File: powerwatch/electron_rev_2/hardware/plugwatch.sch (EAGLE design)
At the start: 73 parts, among them J1 TC2030-JLINK-NL, Q1 MPSA42, T1 DMG3415, U1 MAX-M8, U2 microSD, U3 ISL29035, U37 MPU-9250, U4 NRF51822QF, U5 SAFFB1G56KB0F0A, U6 BGA725L6-ALT, U7 OPA322AIDBVT, X3 16MHz, X4 ABS05-32.768KHZ-9-T

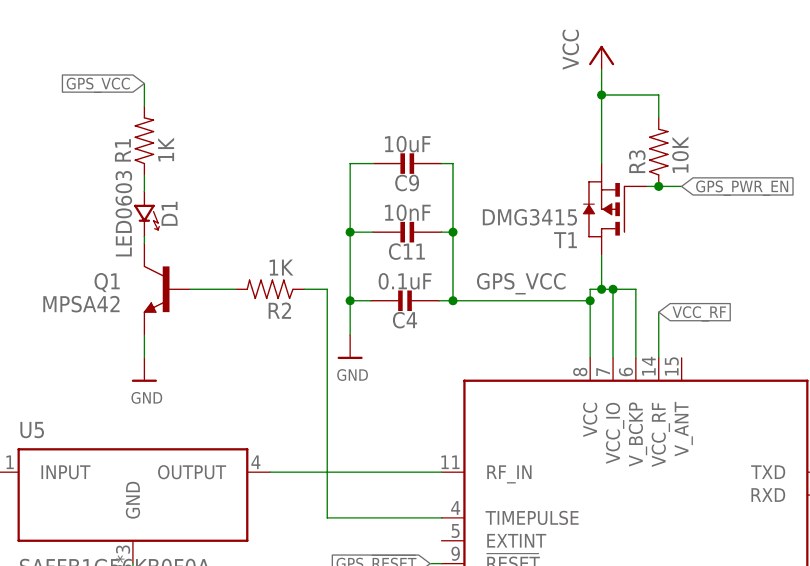
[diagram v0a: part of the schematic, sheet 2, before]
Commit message: Added part numbers and notes
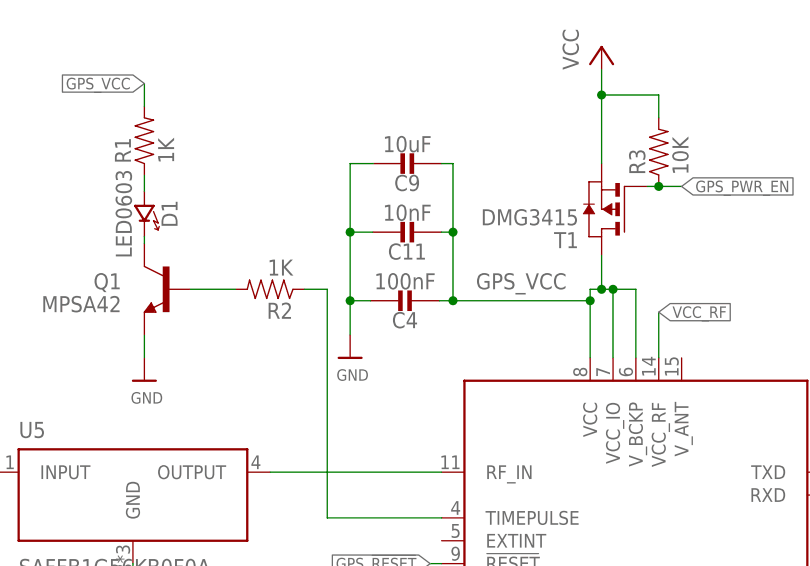
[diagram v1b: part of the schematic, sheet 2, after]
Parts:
- C1, C732: DIGIKEY (none) -> 490-10777-1-ND
- C11, C3, C5: DIGIKEY (none) -> 490-7763-1-ND
- C18: value 0.1uF -> 100nF; DIGIKEY 445-4952-1-ND -> 490-10777-1-ND
- C19, C24: DIGIKEY 490-1303-1-ND -> 490-6366-1-ND
- C2: DIGIKEY (none) -> 445-5947-1-ND
- C21: DIGIKEY 1276-1513-1-ND -> 490-14457-1-ND
- C25: DIGIKEY 445-1264-1-ND -> 490-11420-1-ND
- C4: value 0.1uF -> 100nF; DIGIKEY (none) -> 490-10777-1-ND
- C9: DIGIKEY (none) -> 490-8316-1-ND
- R1, R2: DIGIKEY (none) -> RMCF0402FT1K00CT-ND
- R10, R11, R3, R5, R6, R7, R8: DIGIKEY (none) -> RMCF0402FT10K0CT-ND
- R12: DIGIKEY RHM12.0KCDCT-ND -> RMCF0402FT12K0CT-ND
- R13: DIGIKEY RHM1.0KCECT-ND -> RMCF0402FT1K00CT-ND
- R14: DIGIKEY RHM150CDCT-ND -> RMCF0402FT150RCT-ND
- R15, R9: DIGIKEY 1276-3431-1-ND -> RMCF0402FT10K0CT-ND; MPN MF-RES-0402-10K -> (none); MPN1 RC1005F103CS -> (none)
- R4: DIGIKEY (none) -> RMCF0402FT1M00CT-ND
- T1: DIGIKEY (none) -> DMG3415UDICT-ND
- U37: DIGIKEY (none) -> 1428-1019-1-ND
- U6: DIGIKEY (none) -> BGA725L6E6327FTSA1CT-ND
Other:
- note added: "XXX: Add headers to this part number"
- note added: "XXX: Determine SD part number"
- note added: "XXX: Figure out which FB & GPS to buy"
- note added: "XXX: Find part number for GPS antenna & Inductor"
- note added: "XXX: Need to pick a purchaseable SAW"
- note added: "XXX: Need to pick a purchaseable transistor"
- note added: "XXX: Pick all of these parts"

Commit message: Schematic almost ready
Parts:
- removed Q1: MPSA42, SparkFun-DiscreteSemi:TRANSISTOR_NPNMPSA42
- removed U$3: SIP32510, chips:SIP32510
- removed U$5: CMB-6544PF, microphone:CMB-6544PF
- removed U2: microSD, SparkFun:USD-SOCKETSMD
- added A4: WRL-13678, chips:WRL-13678
- added C12, C13: 100nF, passives:CAPACITOR0402_CAP
- added C15: 330pF, passives:CAPACITOR0402_CAP
- added J2: DM3AT-SF-PEJM5, connector:DM3AT-SF-PEJM5
- added MK1: AOM-4546P-R, microphones:AOM-4546P-R
- added S1: PTS645SM43SMTR92, switches:PTS645SM43SMTR92
- added SW7: SIP3240X, signpost:SIP3240X
- added U8: MAX740XESA, chips:MAX740XESA
- A1: DIGIKEY (none) -> S7051-ND,S7051-ND
- A2: DIGIKEY (none) -> 311-1531-ND
- C10: value 1uf -> 2.2uF; device passives:CAPACITOR0402_CAP -> passives:CAP_POL1206; DIGIKEY (none) -> 718-1131-1-ND
- C6: device passives:CAPACITOR0402_CAP -> passives:CAP_POL1206; DIGIKEY (none) -> 718-1131-1-ND
- C7: value 16pF -> 4.4pF; device passives:CAPACITOR0402_CAP -> passives:CAPACITOR0603_CAP; DIGIKEY (none) -> 399-16187-1-ND
- C8: value 25uF -> 10uF; device passives:CAPACITOR0402_CAP -> passives:CAP_POL1206; DIGIKEY (none) -> 478-8481-1-ND
- L1: DIGIKEY (none) -> 490-11766-1-ND
- L2, L3: value (none) -> 1k; DIGIKEY (none) -> 490-4003-1-ND
- R1: value 1K -> 1k
- R10, R11, R3, R5: value 10K -> 10k
- R16: value 13.7K -> 3.48k; device passives:RESISTOR0402_RES -> passives:RESISTOR0603_RES; DIGIKEY (none) -> 541-3.48KHCT-ND
- R17, R18, R19: value 100K -> 100k; device passives:RESISTOR0402_RES -> passives:RESISTOR0603_RES; DIGIKEY (none) -> 541-2972-1-ND
- R2: value 1K -> 10k; DIGIKEY RMCF0402FT1K00CT-ND -> RMCF0402FT10K0CT-ND
- R20: device passives:RESISTOR0402_RES -> passives:RESISTOR0603_RES; DIGIKEY (none) -> 541-3003-1-ND
- R21: value 75K -> 270k; device passives:RESISTOR0402_RES -> passives:RESISTOR0603_RES; DIGIKEY (none) -> 541-270KHCT-ND
- R4: value 1M -> 10k; DIGIKEY RMCF0402FT1M00CT-ND -> RMCF0402FT10K0CT-ND
- R6, R7: value 10K -> 100k; DIGIKEY RMCF0402FT10K0CT-ND -> 1276-3432-1-ND
- R8: value 10K -> 150; DIGIKEY RMCF0402FT10K0CT-ND -> RMCF0402FT150RCT-ND
- U1: DIGIKEY (none) -> 672-1003-1-ND
- U5: ABACUS_TECHNOLOGIES (none) -> SAFFB1G56KB0F0A
- U7: device OPA322AIDBVT:OPA322AIDBVT -> opamps:OPA322AIDBVT
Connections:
- net GPS_!RESET renamed !GPS_RESET
- net IMU_SCL renamed SENSORS_SCL
- net IMU_SDA renamed SENSORS_SDA
- removed net N$3: C2.1, R5.2, R6.2, R7.2, R8.2, U$3.VLOAD, U2.VCC
- removed net N$37: Q1.B, R2.2
- removed net NRF_VCC: C18.1, C20.1, J1.VCC, R13.1, U4.VDD
- removed net SD_DET: R8.1, U2.CD1
- removed net SD_EN: R4.1, U$3.EN
- removed net SD_SCK: U2.SCK
- removed net SD_SS: R5.1, U2.CS
- removed net TIMEPULSE: R2.1, U1.TIMEPULSE
- new net !SAFEMODE: R8.2, S1.P$2
- new net !SD_CS: J2.DATA3-CD/CS_N, R4.1
- new net !SD_DETECT: J2.A, R6.1
- new net !WIFI_RESET: A4.!RST
- new net AUDIO_OUT: U8.OUT
- new net N$11: C13.1, U8.COM, U8.OS
- new net N$18: C2.1, J2.VCC, R2.2, R4.2, R5.2, R6.2, SW7.VLOAD
- new net N$6: C15.2, U8.CLK
- new net SD_ENABLE_POWER: R7.1, SW7.EN
- new net SD_SCLK: J2.CLK
- new net WIFI_RXD: A4.RXI
- new net WIFI_TXD: A4.TXO
- net -AMP: now also C8.CATHODE; no longer C8.2
- net A_MIC_OUT: now also C10.ANODE, U8.IN; no longer C10.2
- net GND: now also A4.GND, C12.2, C13.2, C15.1, C6.ANODE, J2.B, J2.GND, MK1.2, S1.P$1, SW7.GND, U8.GND; no longer C6.2, Q1.E, U$3.GND, U$5.V-, U2.CD2, U2.GND, U2.SHIELD1, U2.SHIELD2
- net N$2: now also U1.TIMEPULSE; no longer Q1.C
- net N$4: now also C8.ANODE, MK1.1; no longer C8.1, U$5.V+
- net N$7: now also C10.CATHODE; no longer C10.1
- net N$9: now also C6.CATHODE; no longer C6.1
- net SD_MISO: now also J2.DATA0/MISO, R5.1; no longer R7.1, U2.DO
- net SD_MOSI: now also J2.CMD/MOSI, R2.1; no longer R6.1, U2.DI
- net VCC: now also A4.3V3, A4.EN, C18.1, C20.1, J1.VCC, R13.1, R7.2, R8.1, SW7.VSUPP, U4.VDD; no longer R4.2, U$3.VSUPP
- net VCC_A_MIC: now also C12.1, U8.!SHDN, U8.VDD
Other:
- note added: "I2C Address: 0x68"
- note added: "SD Card Adapter"
- note added: "XXX: Check PCB layout section of TI doc"
- note added: "XXX: Pick an actual LED part and apply to other LEDs too"
- note added: "http://www.ti.com/lit/ug/tidu765/tidu765.pdf"
- note added: "https://cdn.sparkfun.com/datasheets/Wireless/WiFi/ESP8266ModuleV1.pdf"
- note added: "https://www.u-blox.com/sites/default/files/MAX-8-M8-FW3_HardwareIntegrationManual_%28UBX-15030059%29.pdf"
- note removed: "SD Card"
- note removed: "XXX: ADD LOW PASS FILTER"
- note removed: "XXX: Add headers to this part number"
- note removed: "XXX: Determine SD part number"
- note removed: "XXX: Figure out which FB & GPS to buy"
- note removed: "XXX: Find part number for GPS antenna & Inductor"
- note removed: "XXX: Need to pick a purchaseable SAW"
- note removed: "XXX: Need to pick a purchaseable transistor"
- note removed: "XXX: Pick all of these parts"
- moved on the sheet: C2, C7, D1, R1, R16, R17, R18, R19, R20, R21, R4, R5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

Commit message: Schematic done?
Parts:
- removed D3: BLUE, SparkFun-LED:LED0603
- added D2: LED0603, leds:LED0603
- added R22: 10k, passives:RESISTOR0402_RES
- added T2: DMG3415, zetex:PMOSSOT23
- D1: DIGIKEY (none) -> 160-1837-6-ND
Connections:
- removed net IMU_INT: R15.1, U37.INT
- new net !IMU_INT: A1.D0, R15.1, U37.INT
- new net AUDIO_PWR_EN: A1.B0, R22.1, T2.G
- net !GPS_RESET: now also A1.D4
- net !LIGHT_INT: now also A1.D1
- net !SAFEMODE: now also A1.D7
- net !SD_CS: now also A1.A2
- net !SD_DETECT: now also A1.D6
- net !WIFI_RESET: now also A1.D5
- net AUDIO_OUT: now also A1.B2
- net BLE_RXD: now also A1.C1
- net BLE_TXD: now also A1.C0
- net GND: now also A1.GND, A1.GND@2
- net GPS_PWR_EN: now also A1.D3
- net GPS_RXD: now also A1.TX
- net GPS_TXD: now also A1.RX
- net N$25: now also D2.ANODE; no longer D3.A
- net NRF_P29: now also D2.CATHODE; no longer D3.C
- net NRF_SWDIO/!RESET: now also A1.D2
- net SD_MISO: now also A1.A4
- net SD_MOSI: now also A1.A5
- net SD_SCLK: now also A1.A3
- net SENSORS_SCL: now also A1.C5
- net SENSORS_SDA: now also A1.C4
- net VCC: now also A1.3V3, R22.2, T2.S
- net VCC_A_MIC: now also T2.D
- net WIFI_RXD: now also A1.C3
- net WIFI_TXD: now also A1.C2
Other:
- note added: "Note: GPIO choices are arbitrary"
- note added: "Note: Pin choices are arbitrary"
- note removed: "XXX: Pick an actual LED part and apply to other LEDs too"
- note removed: "XXX: Pick real pins for me"
- moved on the sheet: C10, C12, C13, C15, C6, C7, C8, MK1, R16, R17, R18, R19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

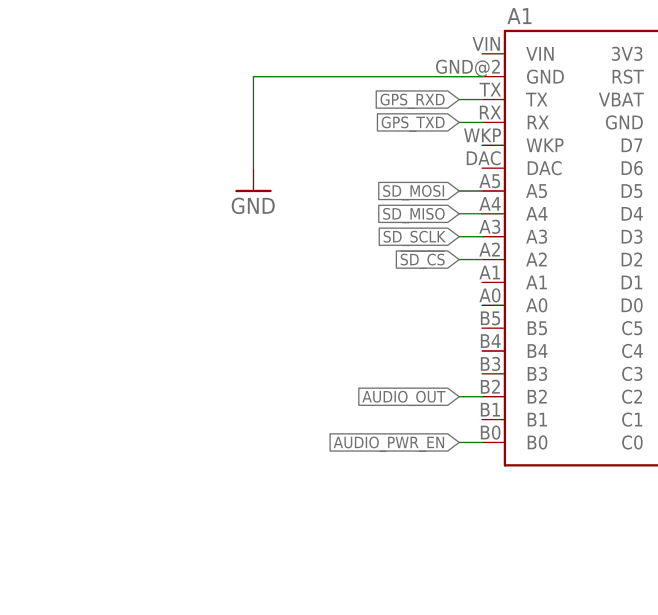
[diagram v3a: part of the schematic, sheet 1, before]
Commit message: locked key parts on board, added LED
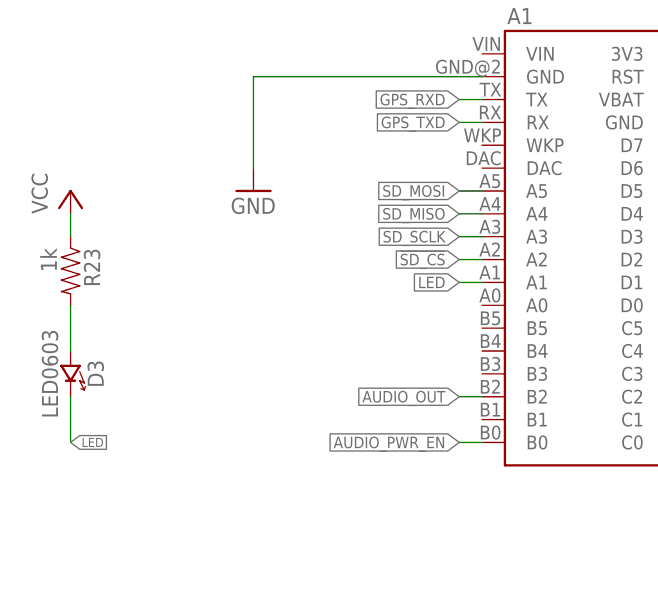
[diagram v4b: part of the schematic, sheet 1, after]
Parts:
- added D3: LED0603, leds:LED0603
- added R23: 1k, passives:RESISTOR0402_RES
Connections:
- new net LED: A1.A1, D3.CATHODE
- new net N$3: D3.ANODE, R23.2
- net VCC: now also R23.1
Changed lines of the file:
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@@
 <part name="P+13" library="supply1" library_urn="urn:adsk.eagle:library:371" deviceset="VCC" device=""/>
 <part name="D2" library="leds" deviceset="LED" device="0603"/>
+<part name="R23" library="passives" deviceset="RESISTOR" device="0402_RES" value="1k">
+<attribute name="DIGIKEY" value="RMCF0402FT1K00CT-ND"/>
+</part>
+<part name="P+14" library="supply1" library_urn="urn:adsk.eagle:library:371" deviceset="VCC" device=""/>
+<part name="D3" library="leds" deviceset="LED" device="0603"/>
 </parts>
 <sheets>
@@
 <instance part="GND32" gate="1" x="121.92" y="127"/>
 <instance part="GND33" gate="1" x="38.1" y="132.08"/>
+<instance part="R23" gate="G$1" x="17.78" y="121.92" rot="R270">
+<attribute name="DIGIKEY" x="17.78" y="121.92" size="1.27" layer="96" rot="R270" display="off"/>
+</instance>
+<instance part="P+14" gate="VCC" x="17.78" y="132.08"/>
+<instance part="D3" gate="G$1" x="17.78" y="111.76" rot="R270"/>
 </instances>
 <busses>
@@
 <wire x1="93.98" y1="147.32" x2="93.98" y2="149.86" width="0.1524" layer="91"/>
 </segment>
+<segment>
+<pinref part="R23" gate="G$1" pin="1"/>
+<pinref part="P+14" gate="VCC" pin="VCC"/>
+<wire x1="17.78" y1="127" x2="17.78" y2="129.54" width="0.1524" layer="91"/>
+</segment>
 </net>
 <net name="!SAFEMODE" class="0">
@@
 </segment>
 </net>
+<net name="N$3" class="0">
+<segment>
+<pinref part="R23" gate="G$1" pin="2"/>
+<pinref part="D3" gate="G$1" pin="ANODE"/>
+<wire x1="17.78" y1="114.3" x2="17.78" y2="119.38" width="0.1524" layer="91"/>
+</segment>
+</net>
+<net name="LED" class="0">
+<segment>
+<pinref part="A1" gate="A1" pin="A1"/>
+<wire x1="63.5" y1="121.92" x2="60.96" y2="121.92" width="0.1524" layer="91"/>
+<label x="60.96" y="121.92" size="1.27" layer="95" rot="R180" xref="yes"/>
+</segment>
+<segment>
+<label x="17.78" y="104.14" size="1.016" layer="95" xref="yes"/>
+<pinref part="D3" gate="G$1" pin="CATHODE"/>
+<wire x1="17.78" y1="109.22" x2="17.78" y2="104.14" width="0.1524" layer="91"/>
+</segment>
+</net>

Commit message: Nothing to do!
Still need to review DRC, clean up signals, and add testpoints.
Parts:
- removed R22: 10k, passives:RESISTOR0402_RES
- removed T1, T2: DMG3415, zetex:PMOSSOT23
- added R24, R25, R26: 100k, passives:RESISTOR0402_RES
- added SW1, SW2, SW3, SW4: SIP3240X, signpost:SIP3240X
- R3: value 10k -> 100k; DIGIKEY RMCF0402FT10K0CT-ND -> 1276-3432-1-ND
- renumbered C732 to C30
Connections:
- new net BLE_PWR_EN: A1.B5, R24.1, SW4.EN
- new net BLE_VCC: R13.1
- new net N$14: A4.3V3, A4.EN, SW3.VLOAD
- new net VCC_BLE: C18.1, C20.1, J1.VCC, SW4.VLOAD, U4.VDD
- new net WIFI_PWR_EN: A1.A0, R26.1, SW3.EN
- net AUDIO_PWR_EN: now also R25.1, SW2.EN; no longer R22.1, T2.G
- net GND: now also SW1.GND, SW2.GND, SW3.GND, SW4.GND
- net GPS_PWR_EN: now also SW1.EN; no longer T1.G
- net GPS_VCC: now also SW1.VLOAD; no longer T1.D, U1.V_BCKP
- net VCC: now also R24.2, R25.2, R26.2, SW1.VSUPP, SW2.VSUPP, SW3.VSUPP, SW4.VSUPP; no longer A4.3V3, A4.EN, C18.1, C20.1, J1.VCC, R13.1, R22.2, T1.S, T2.S, U4.VDD
- net VCC_A_MIC: now also SW2.VLOAD; no longer T2.D
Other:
- moved on the sheet: C11, C4, C9, R3
